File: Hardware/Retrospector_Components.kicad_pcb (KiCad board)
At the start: 4 copper layers, 60 x 110 mm, 143 parts, among them J1 SWD_Header, J2 Eurorack_10_pin_power, J3 Conn_01x08_Male, J4 Conn_01x08_Male, J5 Conn_01x08_Male, J6 Conn_01x08_Male, J7 USB_B_Micro, U1 STM32H743ZITx, U10 LM2675M-5, U11 TL072, U2 IS42S16800F-7TLI, U3 PCM5100APW, U4 AS3364, U5 MCP6004, U6 MCP6004, U7 TL074, U8 LD1117-3.3-4Tab, Y1 8MHz 20pF

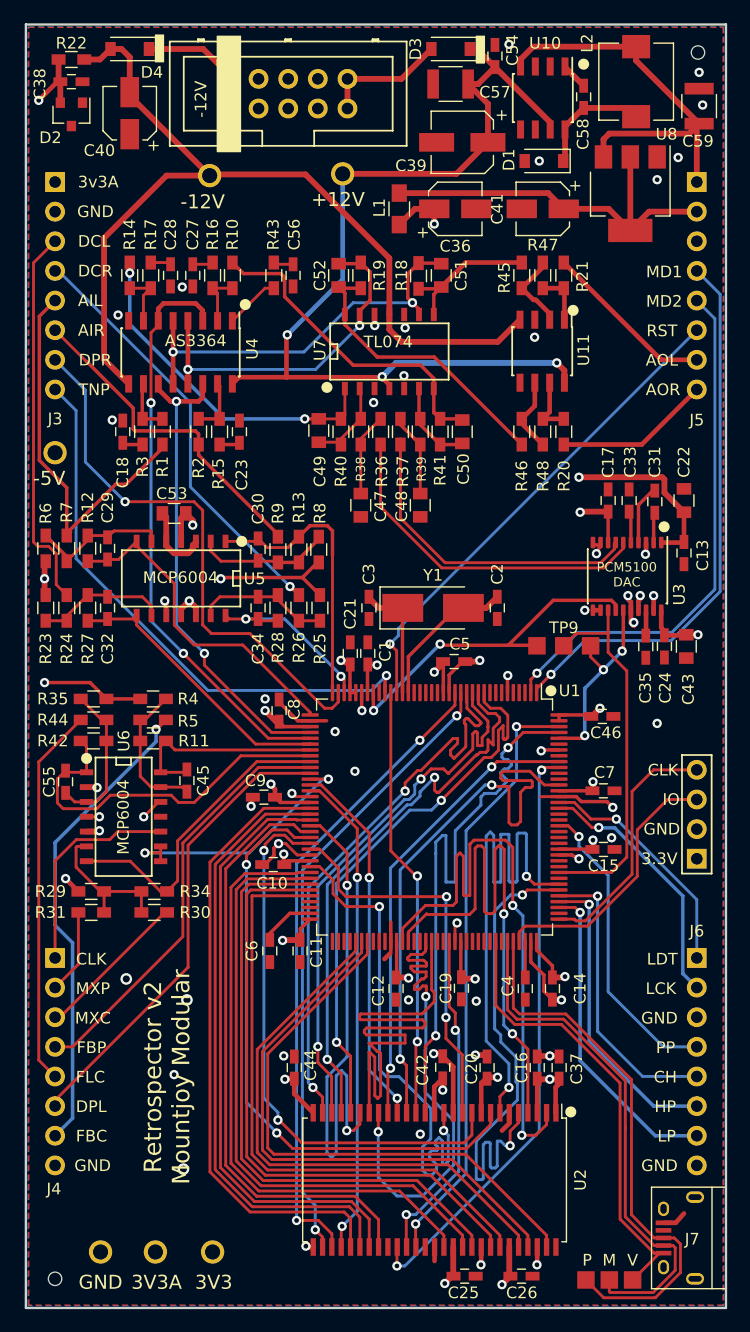
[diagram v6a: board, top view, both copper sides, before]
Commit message: Added cycling test mode to RGB LED; Further updates to PCB layout
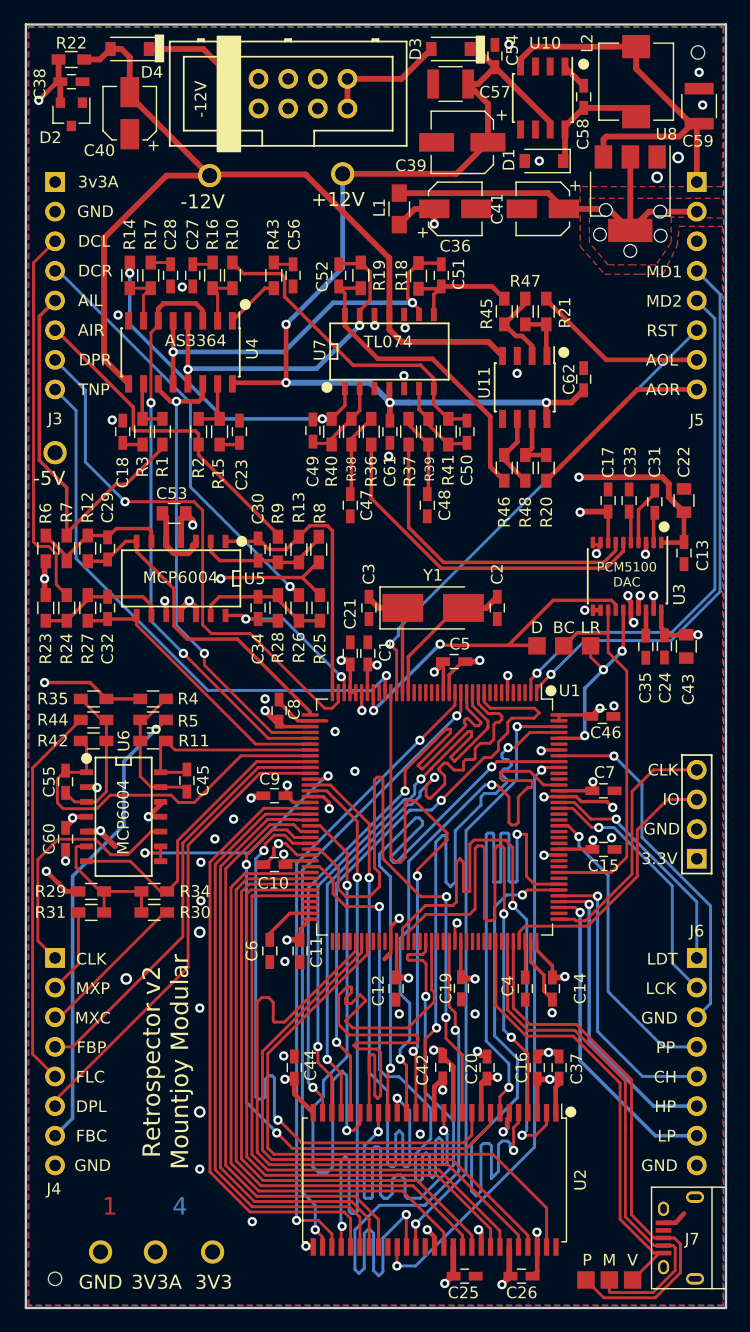
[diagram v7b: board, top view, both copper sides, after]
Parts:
- added C60: 2.2uF, Capacitors_SMD:C_0603_HandSoldering, F.Cu at (103.4, 119.8)
- added C61: 2.2uF, Capacitors_SMD:C_0603_HandSoldering, F.Cu at (131.2, 84.9)
- added C62: 2.2uF, Capacitors_SMD:C_0603_HandSoldering, F.Cu at (147.8, 80.4)
- added REF**: 4_Layer_Markers, Custom_Footprints:4_Layer_Markers, F.Cu at (110.2, 151.3)
- C47, C48, C49, C50, C51, C52: footprint Capacitors_SMD:C_0805 -> Capacitors_SMD:C_0603_HandSoldering
- moved R20 3.44 mm to (144.6, 88.0)
- moved R21 3.44 mm to (144.6, 74.6)
- moved R45 3.44 mm to (141.0, 74.6)
- moved R46 3.44 mm to (141.0, 88.0)
- moved R47 3.44 mm to (142.8, 74.6)
- moved R48 3.44 mm to (142.8, 88.0)
- moved U11 3.44 mm to (142.8, 81.1)
- moved C9 0.91 mm to (121.3, 116.1)
- moved C47 0.90 mm to (127.8, 91.2)
- moved R36 0.80 mm to (129.6, 84.9)
- moved R40 0.80 mm to (126.2, 84.9)
- moved R38 0.80 mm to (127.9, 84.9)
- moved R37 0.70 mm to (132.8, 84.9)
- moved R39 0.70 mm to (134.5, 84.9)
- moved R41 0.70 mm to (136.2, 84.9)
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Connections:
- J6 pad 3: GND -> /LOCK_BTN
- U1 pad 137: Net-(U1-Pad137) -> /LOCK_BTN
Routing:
- net /LOCK_BTN: track 0.00 -> 31.1 mm, vias 0 -> 1
- net /FMC_SDCLK: track 28.9 -> 52.5 mm
- net /FMC_~RAS: track 31.7 -> 51.3 mm
- net /FMC_D6: track 33.6 -> 52.0 mm
- net /FMC_SD~WE: track 37.0 -> 50.4 mm
- net /FMC_SD~E1: track 39.3 -> 50.2 mm
- net /FMC_A6: track 41.8 -> 52.2 mm
- net /FMC_BA0: track 41.0 -> 51.0 mm
- net /FMC_BA1: track 46.2 -> 53.3 mm
- net GND: track 80.1 -> 86.3 mm, vias 54 -> 66
- net /FMC_D2: track 45.0 -> 50.3 mm
- net /FMC_D5: track 48.2 -> 53.4 mm
- net /FMC_A3: track 49.1 -> 54.2 mm
- net /FMC_D13: track 47.9 -> 53.0 mm
- net /FMC_D7: track 46.3 -> 51.1 mm
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- added copper zone on F.Cu, net +3V3
- added copper zone on Power.Rails, net GND
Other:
- board text added: "BC"
- board text added: "D"
- board text added: "LR"
- board text added: "To Do: Ground Vias Opamp decoupling caps Widen traces"
- board text removed: "To Do: Thermal Vias on LDO Ground Vias Opamp decoupling caps Ground under MCU/RAM Layer indicator Widen traces Length match RAM"

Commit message: PCB Clean up
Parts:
- added TP13: TestPoint, Measurement_Points:Measurement_Point_Square-SMD-Pad_Small, F.Cu at (157.8, 110.7)
- added TP14: TestPoint, Measurement_Points:Measurement_Point_Square-SMD-Pad_Small, F.Cu at (154.2, 110.7)
- moved TP5 4.85 mm to (122.3, 63.0)
- moved TP4 1.80 mm to (104.3, 86.8)
- moved J1 1.20 mm to (157.5, 122.7)
- moved C18 0.70 mm to (109.0, 84.9)
- moved C23 0.70 mm to (119.0, 84.9)
- moved C27 0.70 mm to (115.0, 71.5)
- moved R1 0.70 mm to (112.4, 84.9)
- moved R10 0.70 mm to (118.4, 71.5)
- moved R15 0.70 mm to (117.3, 84.9)
- moved R16 0.70 mm to (116.7, 71.5)
- moved R17 0.70 mm to (111.4, 71.5)
- moved R2 0.70 mm to (115.5, 84.9)
- moved R3 0.70 mm to (110.7, 84.9)
- moved U4 0.70 mm to (114.0, 78.1)
- moved C28 0.70 mm to (113.1, 71.5)
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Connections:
- U1 pad 134: Net-(U1-Pad134) -> /LOCK_BTN
- U1 pad 137: /LOCK_BTN -> /I2C1_SDA
- U1 pad 139: Net-(U1-Pad139) -> /I2C1_SCL
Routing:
- net /I2C1_SDA: track 0.00 -> 13.0 mm, vias 0 -> 2
- net /I2C1_SCL: track 0.00 -> 8.98 mm, vias 0 -> 2
- net /LOCK_BTN: track 31.1 -> 28.9 mm
- net /-5V_REF: track 116.4 -> 118.2 mm, vias 5 -> 8
- net VCC: track 88.0 -> 89.7 mm
- net /DAC_OUT_AMP_R: track 27.8 -> 29.2 mm
- net GND: track 86.3 -> 87.4 mm, vias 66 -> 199
- net +3V3: track 116.6 -> 115.5 mm
- net Net-(R43-Pad2): track 5.16 -> 4.20 mm
- net /LED_SPI_CLK: track 22.1 -> 21.3 mm
- net /DELAY_CV_R: track 36.6 -> 37.4 mm
- net /SWCLK: track 21.4 -> 20.7 mm
- net /DRY_OUT_R: track 29.8 -> 29.1 mm
- net /DAC_OUT_AMP_L: track 29.7 -> 29.1 mm
- net /DRY_OUT_L: track 35.2 -> 34.5 mm
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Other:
- board text added: "3VA"
- board text added: "C"
- board text added: "DAC"
- board text added: "LKB"
- board text added: "MCU"
- board text added: "SDRAM"
- board text added: "To Do: Ground Vias"
- board text removed: "3v3A"
- board text removed: "J4"
- board text removed: "To Do: Ground Vias Opamp decoupling caps Widen traces"
